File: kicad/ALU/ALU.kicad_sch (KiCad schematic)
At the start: 85 parts, among them J1 Control Connector, J10 Backplane Signal, J2 Data Connector, J20 Backplane Bus, U1 74LS377, U10 74LS253, U11 74LS253, U12 74LS253, U13 74LS253, U14 74LS253, U15 74LS253, U16 74LS253, U17 74F382, U18 74F382, U19 74F382, U2 74LS377, U20 74F382, U21 74F382, U22 74LS283, U23 74LS283, U24 74LS283, U25 74LS283, U26 74LS283, U27 74LS244, U28 74LS244, U29 74LS244, U3 74LS377, U30 74LS386, U31 74LS08, U32 74LS32, U33 74LS04, U34 74LS253, U35 74LS27, U36 74LS27, U37 74LS11, U38 74LS257, U39 74LS32, U4 74LS377, U5 74LS377, U6 74LS377, U7 74LS253, U8 74LS253, U9 74LS253

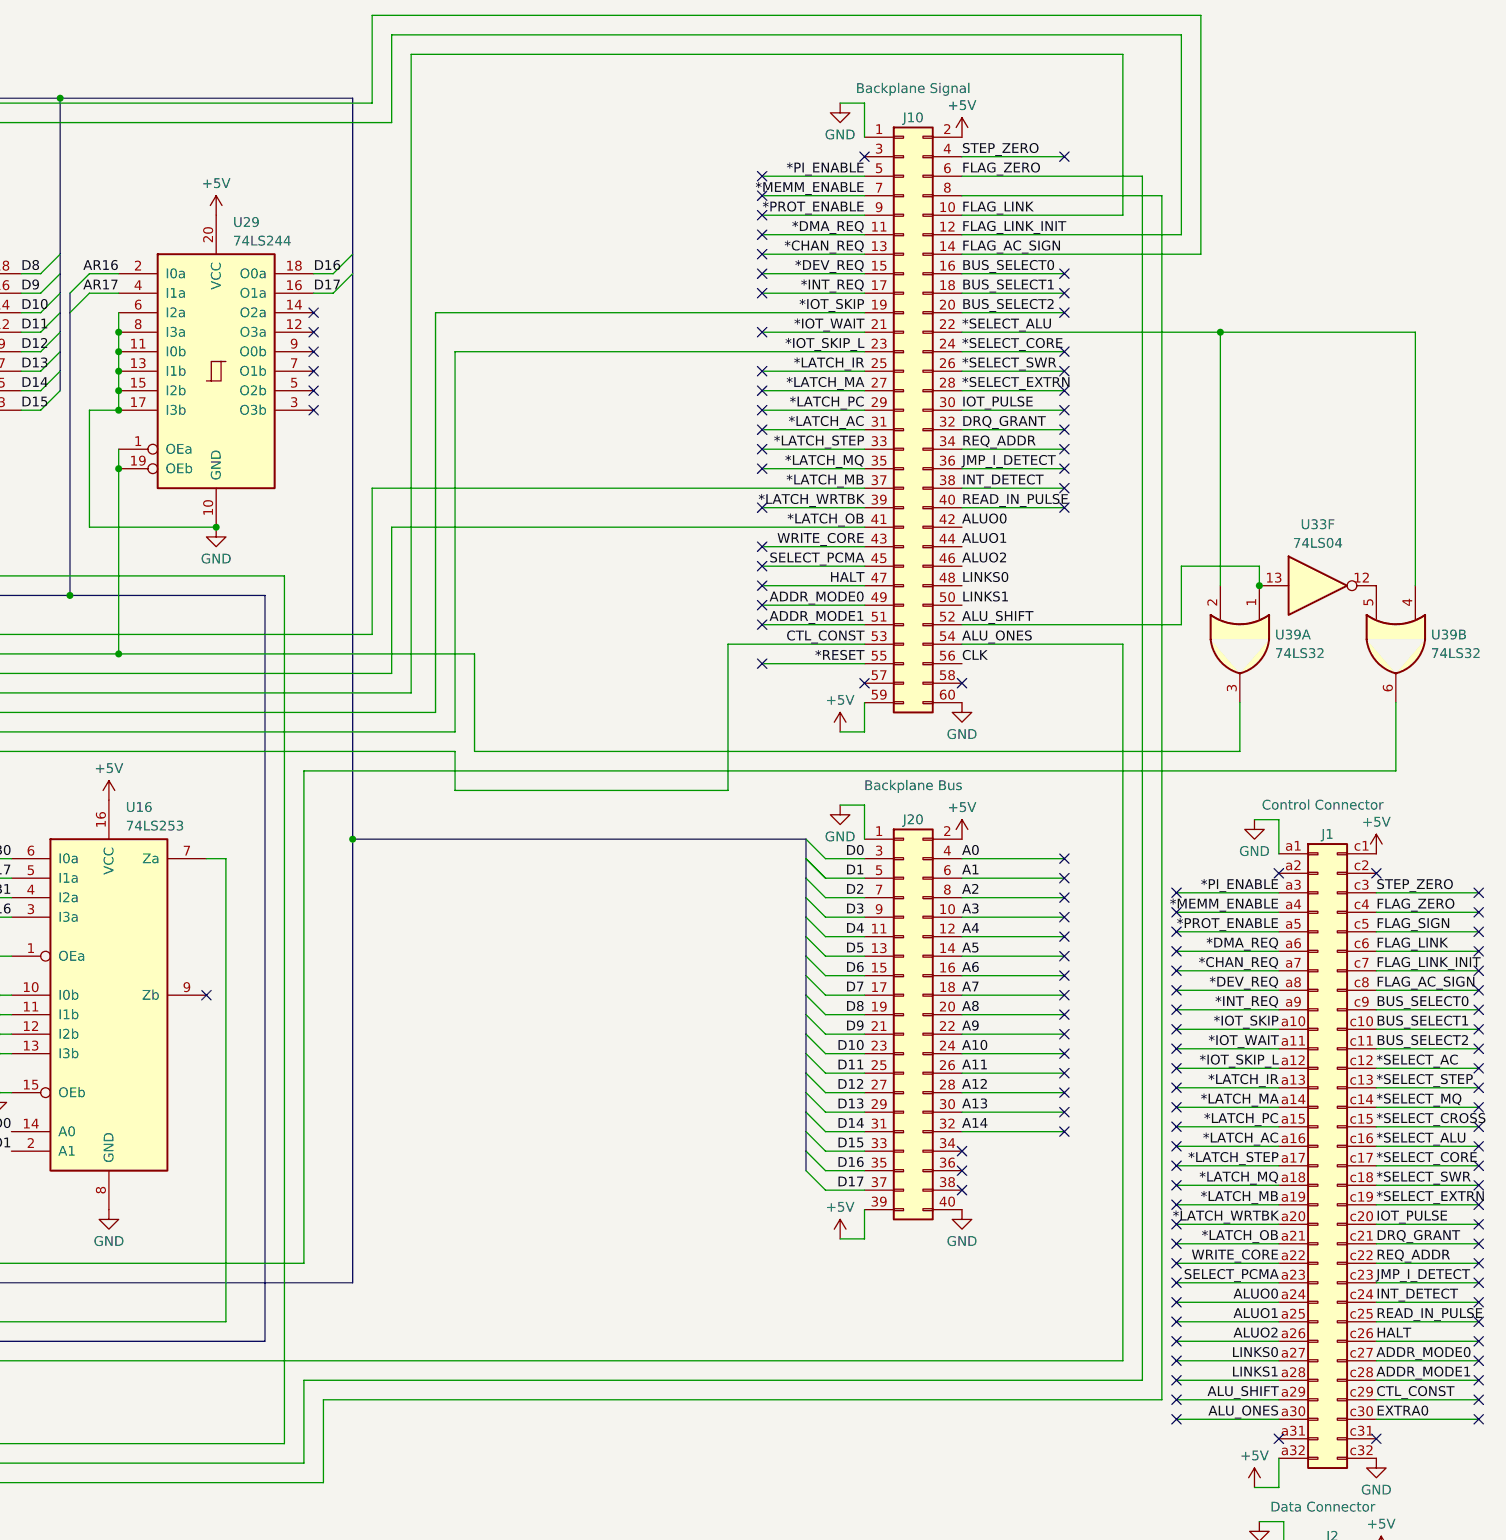
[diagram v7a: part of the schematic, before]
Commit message: Continue connector migration
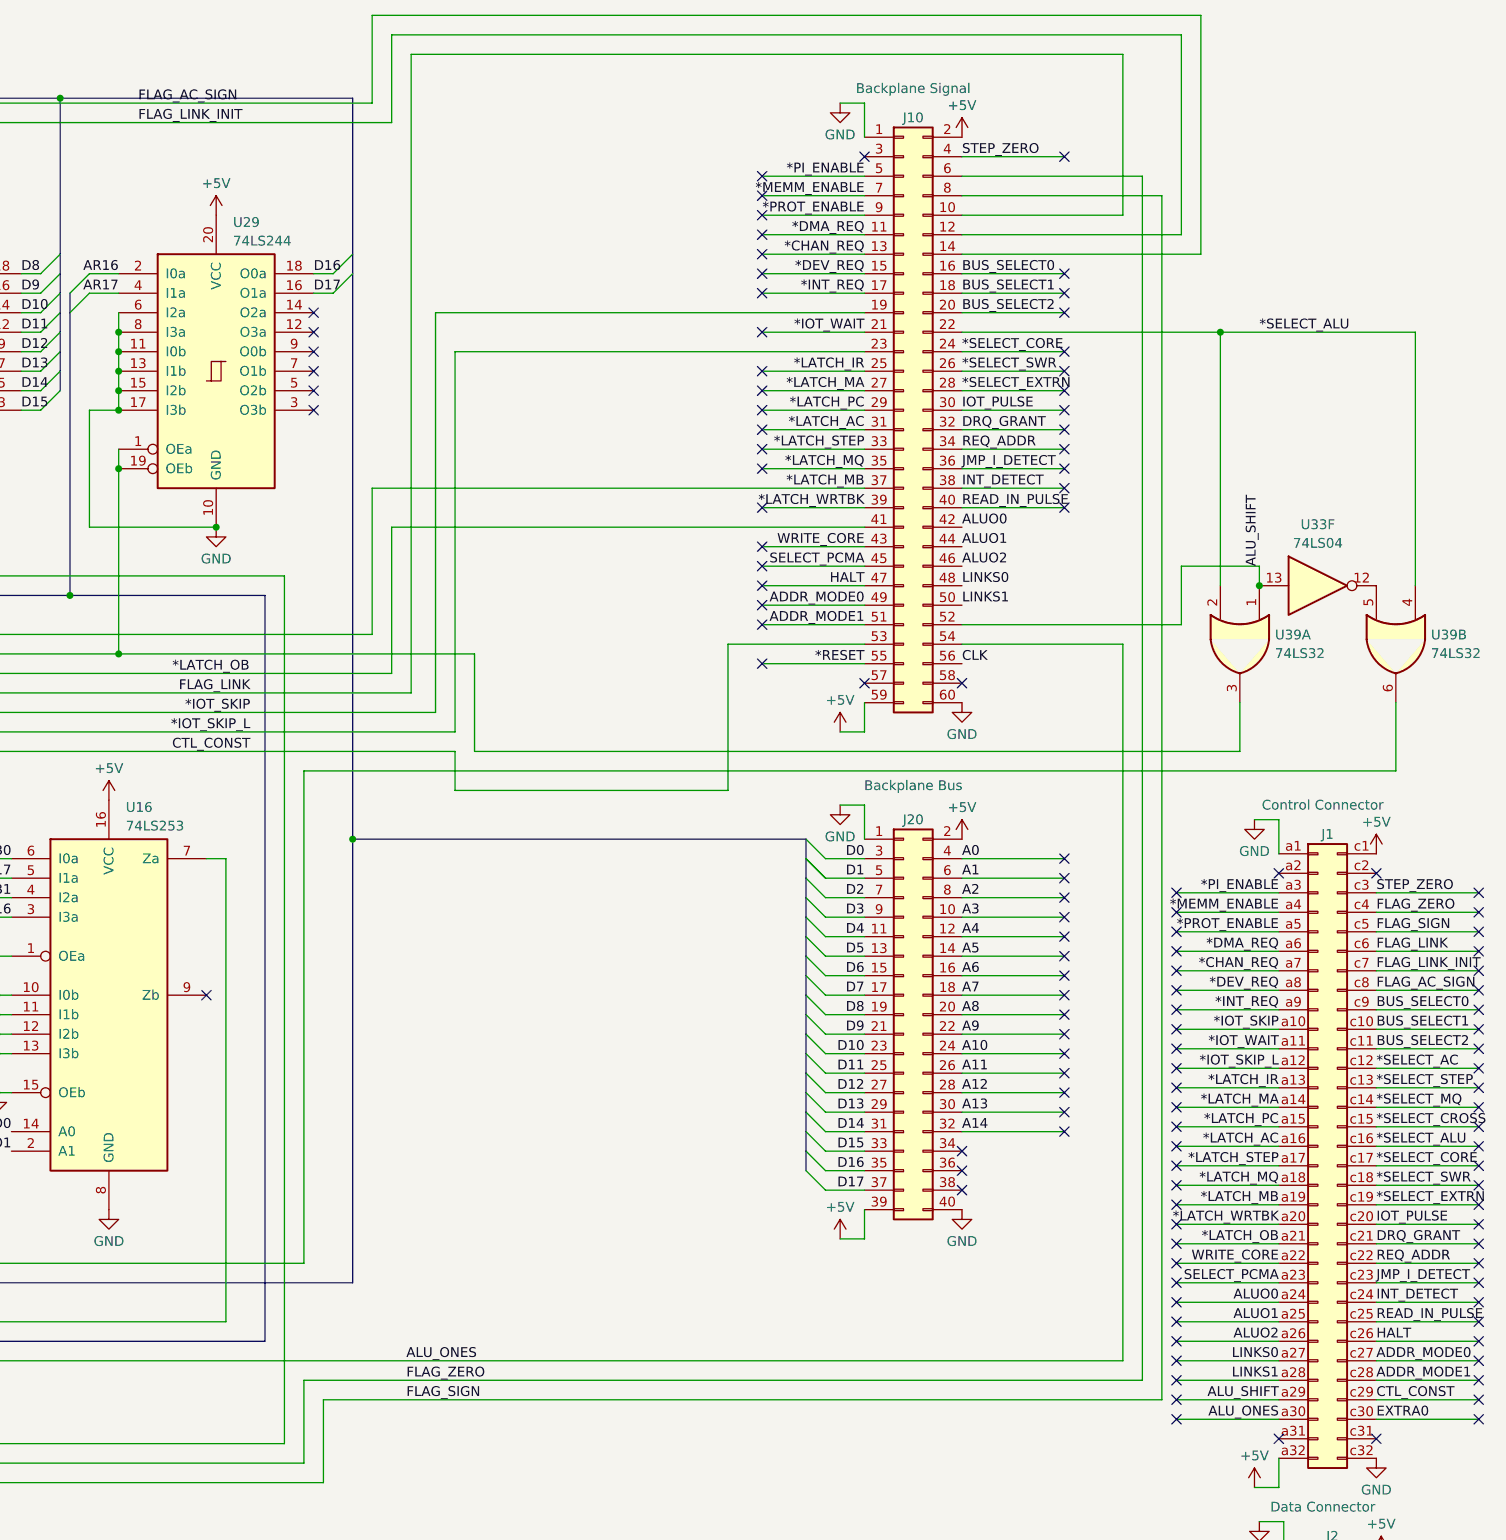
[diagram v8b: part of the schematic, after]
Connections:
- net OB17 is gone; now on net FLAG_SIGN: J10.8 (Pin_8), U14.12 (I2b), U15.6 (I0a), U16.5 (I1a), U21.1 (A1), U3.5 (Q1), U30.6, U33.3, U36.11, U7.3 (I3a)
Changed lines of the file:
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@@
     (effects (font (size 1.27 1.27)) (justify right bottom))
+  )
+  (label "FLAG_SIGN" (at 441.325 193.675 0) (fields_autoplaced)
+    (effects (font (size 1.27 1.27)) (justify left bottom))
   )
   (label "OB7" (at 64.77 64.77 180) (fields_autoplaced)
@@
     (effects (font (size 1.27 1.27)) (justify left bottom))
   )
-  (label "*SELECT_ALU" (at 513.715 54.61 0) (fields_autoplaced)
+  (label "*SELECT_ALU" (at 552.45 54.61 0) (fields_autoplaced)
     (effects (font (size 1.27 1.27)) (justify left bottom))
   )
@@
     (effects (font (size 1.27 1.27)) (justify right bottom))
   )
-  (label "FLAG_ZERO" (at 513.715 34.29 0) (fields_autoplaced)
+  (label "FLAG_ZERO" (at 441.325 191.135 0) (fields_autoplaced)
     (effects (font (size 1.27 1.27)) (justify left bottom))
   )
@@
     (effects (font (size 1.27 1.27)) (justify right bottom))
   )
-  (label "ALU_ONES" (at 513.715 95.25 0) (fields_autoplaced)
+  (label "ALU_ONES" (at 441.325 188.595 0) (fields_autoplaced)
     (effects (font (size 1.27 1.27)) (justify left bottom))
   )
@@
     (effects (font (size 1.27 1.27)) (justify left bottom))
   )
-  (label "ALU_SHIFT" (at 513.715 92.71 0) (fields_autoplaced)
+  (label "ALU_SHIFT" (at 552.45 85.09 90) (fields_autoplaced)
     (effects (font (size 1.27 1.27)) (justify left bottom))
   )
@@
     (effects (font (size 1.27 1.27)) (justify right bottom))
   )
-  (label "CTL_CONST" (at 501.015 95.25 180) (fields_autoplaced)
+  (label "CTL_CONST" (at 421.005 109.22 180) (fields_autoplaced)
     (effects (font (size 1.27 1.27)) (justify right bottom))
   )
@@
     (effects (font (size 1.27 1.27)) (justify left bottom))
   )
-  (label "FLAG_AC_SIGN" (at 513.715 44.45 0) (fields_autoplaced)
+  (label "FLAG_AC_SIGN" (at 406.4 24.765 0) (fields_autoplaced)
     (effects (font (size 1.27 1.27)) (justify left bottom))
   )
@@
     (effects (font (size 1.27 1.27)) (justify right bottom))
   )
-  (label "*LATCH_OB" (at 501.015 80.01 180) (fields_autoplaced)
-    (effects (font (size 1.27 1.27)) (justify right bottom))
+  (label "*LATCH_OB" (at 410.845 99.06 0) (fields_autoplaced)
+    (effects (font (size 1.27 1.27)) (justify left bottom))
   )
   (label "IOT_PULSE" (at 513.715 64.77 0) (fields_autoplaced)
@@
     (effects (font (size 1.27 1.27)) (justify right bottom))
   )
-  (label "FLAG_LINK_INIT" (at 513.715 41.91 0) (fields_autoplaced)
+  (label "FLAG_LINK_INIT" (at 406.4 27.305 0) (fields_autoplaced)
     (effects (font (size 1.27 1.27)) (justify left bottom))
   )
@@
     (effects (font (size 1.27 1.27)) (justify left bottom))
   )
-  (label "*IOT_SKIP_L" (at 501.015 57.15 180) (fields_autoplaced)
+  (label "*IOT_SKIP_L" (at 421.005 106.68 180) (fields_autoplaced)
     (effects (font (size 1.27 1.27)) (justify right bottom))
   )
@@
     (effects (font (size 1.27 1.27)) (justify right bottom))
   )
-  (label "*IOT_SKIP" (at 501.015 52.07 180) (fields_autoplaced)
+  (label "*IOT_SKIP" (at 421.005 104.14 180) (fields_autoplaced)
     (effects (font (size 1.27 1.27)) (justify right bottom))
   )
@@
     (effects (font (size 1.27 1.27)) (justify left bottom))
   )
-  (label "FLAG_LINK" (at 513.715 39.37 0) (fields_autoplaced)
-    (effects (font (size 1.27 1.27)) (justify left bottom))
+  (label "FLAG_LINK" (at 421.005 101.6 180) (fields_autoplaced)
+    (effects (font (size 1.27 1.27)) (justify right bottom))
   )
   (label "D3" (at 172.72 54.61 0) (fields_autoplaced)
